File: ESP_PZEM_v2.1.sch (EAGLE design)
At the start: 31 parts, among them IC1 ESP01S, IC3 74HC4052D, Q1 BSS138, Q2 BSS138, U1 LM1117-3.3, X1 KF301-5.0-2P, X2 S4B-XH-A-1, X3 S4B-XH-A-1, X4 S4B-XH-A-1, X5 S4B-XH-A-1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

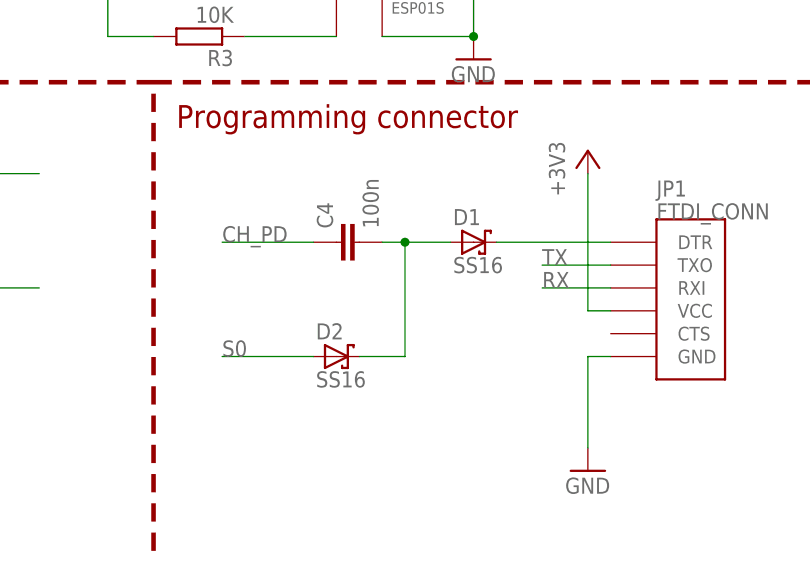
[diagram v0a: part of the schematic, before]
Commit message: SS16 -> BAT54C
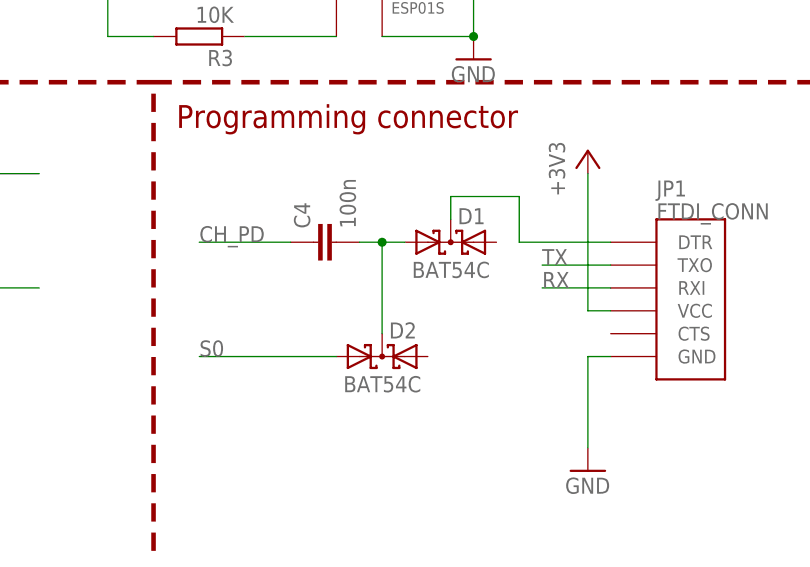
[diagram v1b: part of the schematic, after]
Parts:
- D1, D2: value SS16 -> BAT54C; device my-diode:SS16 -> diode:BAT54C
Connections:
- net N$2: now also D1.A1, D2.CC; no longer D1.A, D2.C
- net N$8: now also D1.CC; no longer D1.C
- net S0: now also D2.A1; no longer D2.A
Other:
- moved on the sheet: C4
